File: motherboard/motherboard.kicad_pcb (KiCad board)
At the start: 2 copper layers, 79.8 x 53.3 mm, 54 parts, among them J1 locked, J2 PROGRAM, J3 Battery / Pitot/ Orientation, J4 c02 censor, J5 shaftencorder, J6 USB_C_Receptacle_USB2.0, J7 SparLoad, J8 lidar, J9 Control Board, Q1 2N7002K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

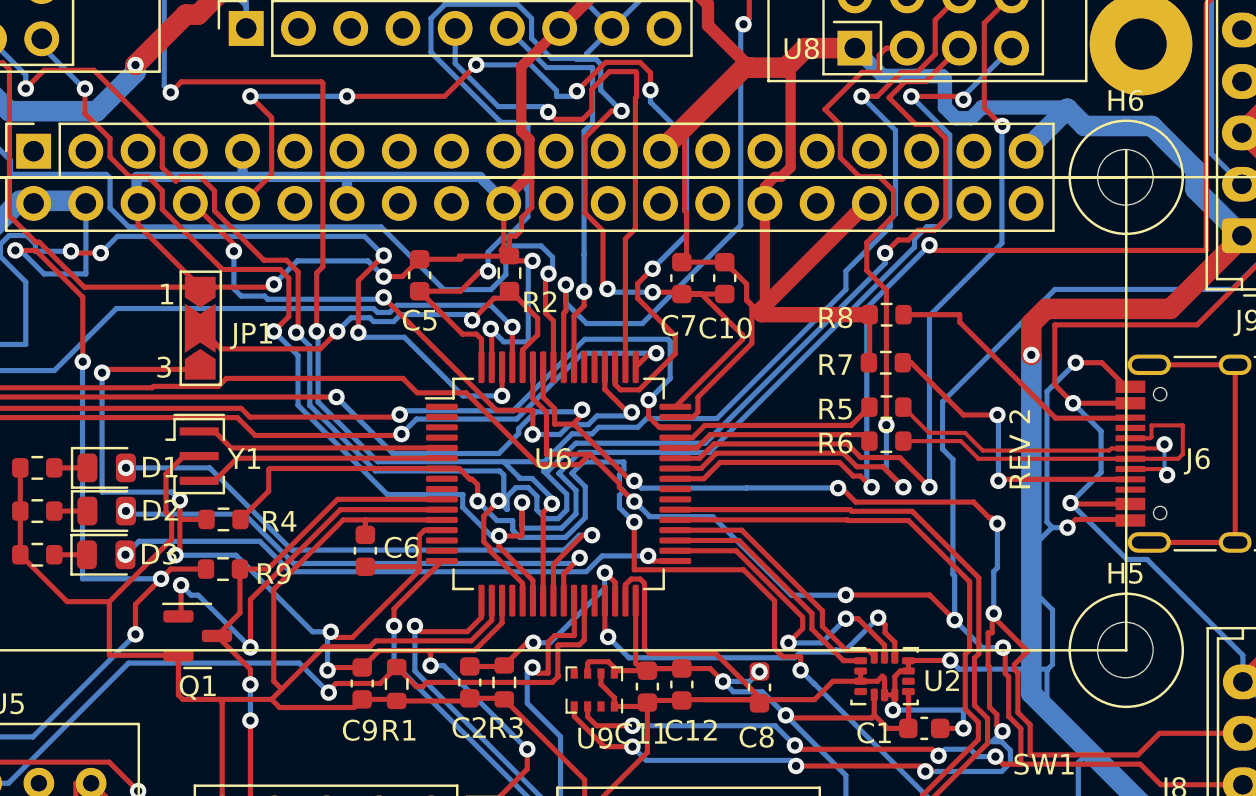
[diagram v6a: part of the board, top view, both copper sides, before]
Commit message: Fixed USB connections
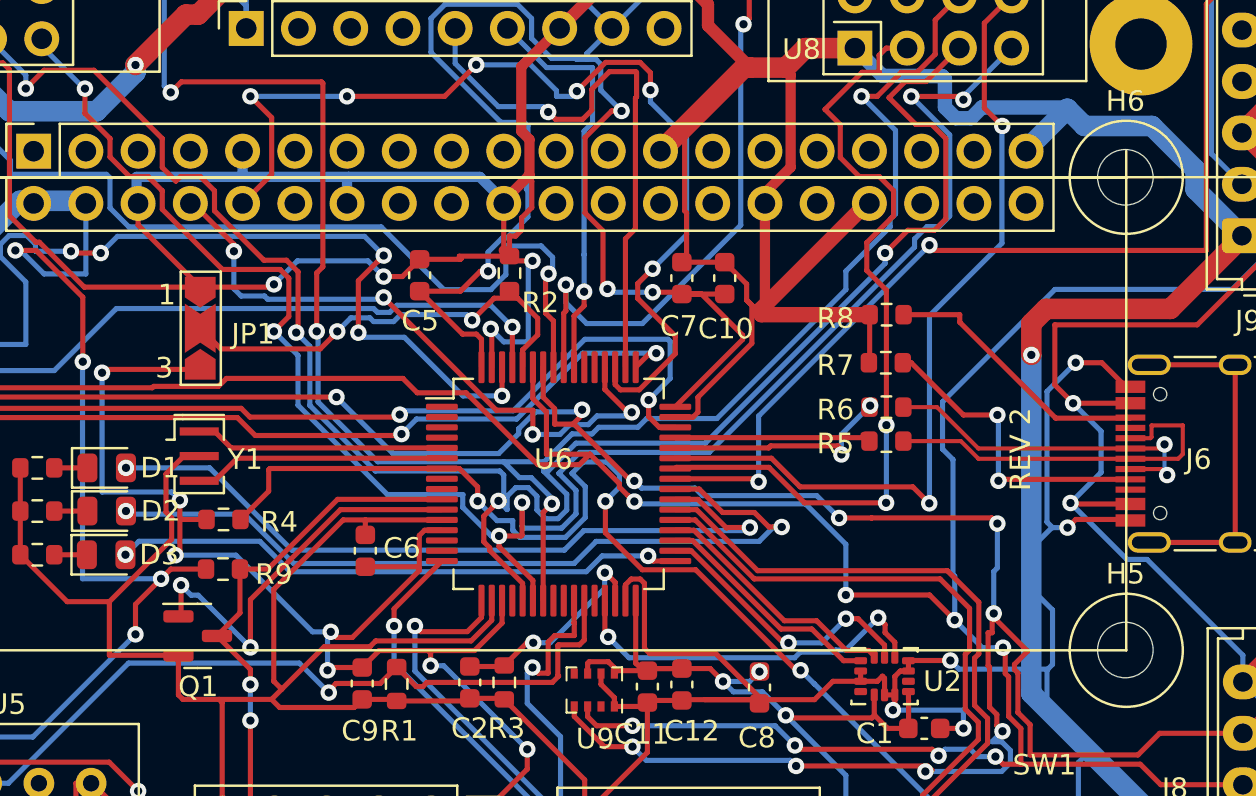
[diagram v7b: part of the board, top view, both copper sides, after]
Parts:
- renumbered R6 to R5, R5 to R6
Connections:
- U6 pad 24: Net-(D1-A) -> unconnected-(U6-PC4-Pad24)
- U6 pad 25: Net-(D2-A) -> unconnected-(U6-PC5-Pad25)
- U6 pad 39: unconnected-(U6-PC8-Pad39) -> Net-(D1-A)
- U6 pad 40: unconnected-(U6-PC9-Pad40) -> Net-(D2-A)
- U6 pad 44: /USB_{D+} -> /USB_{D-}
- U6 pad 45: /USB_{D-} -> /USB_{D+}
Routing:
- net Net-(D2-A): track 25.6 -> 39.6 mm
- net Net-(D1-A): track 28.8 -> 36.7 mm
- net /TELE_{CS}-E: track 68.2 -> 63.8 mm
- net /RST: track 62.9 -> 60.6 mm
- net /SPI2SCK: track 15.4 -> 13.6 mm
- net /USB_{D-}: track 10.1 -> 11.5 mm, vias 0 -> 2
- net /I2C_{SDA}: track 160.2 -> 161.6 mm
- net /USART6_{TX}: track 67.6 -> 66.8 mm
- net /USART6_{RX}: track 72.4 -> 71.7 mm
- net /TELE_{CE}-E: track 39.4 -> 38.7 mm
- net /TELE_{IRQ}-E: track 39.8 -> 40.3 mm
